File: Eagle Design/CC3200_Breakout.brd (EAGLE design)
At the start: 58.4 x 35.2 mm, 46 parts, among them J22 M10X2, J23 M10X2, U15 AT25FS010, Y2 32.768KHz, Y3 407MHz

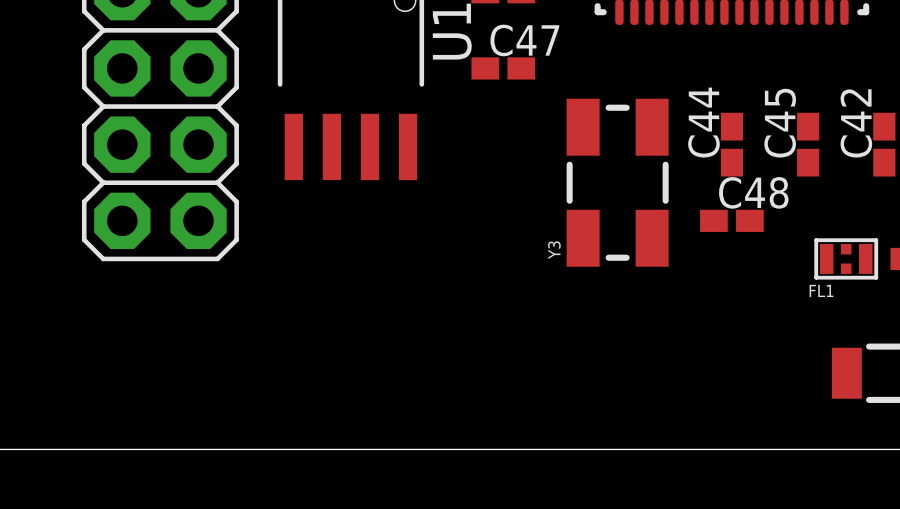
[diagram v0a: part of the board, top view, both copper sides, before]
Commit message: Added JTAG and Lock Connectors
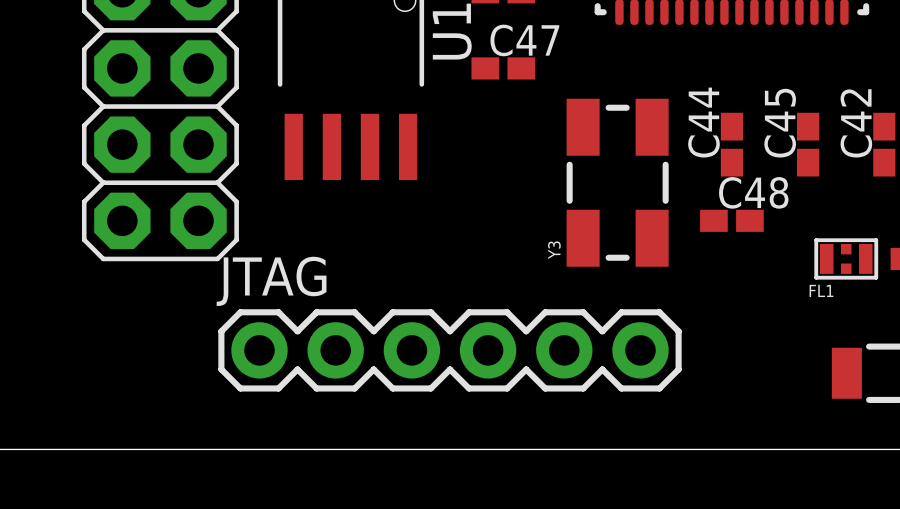
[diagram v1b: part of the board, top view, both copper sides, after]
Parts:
- added JTAG: (no value), SparkFun-Connectors:1X06
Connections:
- net GND: now also JTAG.2
- net JTAG_TCK: now also JTAG.3
- net JTAG_TDI: now also JTAG.5
- net JTAG_TDO: now also JTAG.6
- net JTAG_TMS: now also JTAG.4
- net VCC_BRD: now also JTAG.1
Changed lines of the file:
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@@
 <?xml version="1.0" encoding="utf-8"?>
 <!DOCTYPE eagle SYSTEM "eagle.dtd">
-<eagle version="6.4">
+<eagle version="7.1.0">
 <drawing>
 <settings>
@@
 <layer number="54" name="bGND_GNDA" color="1" fill="9" visible="no" active="no"/>
 <layer number="56" name="wert" color="7" fill="1" visible="no" active="no"/>
+<layer number="57" name="tCAD" color="7" fill="1" visible="no" active="no"/>
+<layer number="90" name="Modules" color="5" fill="1" visible="no" active="no"/>
 <layer number="91" name="Nets" color="2" fill="1" visible="no" active="no"/>
 <layer number="92" name="Busses" color="1" fill="1" visible="no" active="no"/>
@@
 <layer number="97" name="Info" color="7" fill="1" visible="no" active="no"/>
 <layer number="98" name="Guide" color="6" fill="1" visible="no" active="no"/>
+<layer number="99" name="SpiceOrder" color="7" fill="1" visible="no" active="no"/>
 <layer number="100" name="Muster" color="7" fill="1" visible="no" active="no"/>
 <layer number="101" name="Patch_Top" color="12" fill="4" visible="no" active="yes"/>
@@
 <layer number="108" name="tplace-old" color="10" fill="1" visible="yes" active="yes"/>
 <layer number="109" name="ref-old" color="11" fill="1" visible="yes" active="yes"/>
+<layer number="110" name="fp0" color="7" fill="1" visible="yes" active="yes"/>
+<layer number="111" name="LPC17xx" color="7" fill="1" visible="yes" active="yes"/>
+<layer number="112" name="tSilk" color="7" fill="1" visible="yes" active="yes"/>
+<layer number="113" name="IDFDebug" color="4" fill="1" visible="yes" active="yes"/>
 <layer number="116" name="Patch_BOT" color="9" fill="4" visible="no" active="yes"/>
 <layer number="121" name="_tsilk" color="7" fill="1" visible="no" active="yes"/>
 <layer number="122" name="_bsilk" color="7" fill="1" visible="no" active="yes"/>
+<layer number="123" name="tTestmark" color="7" fill="1" visible="yes" active="yes"/>
+<layer number="124" name="bTestmark" color="7" fill="1" visible="yes" active="yes"/>
 <layer number="125" name="_tNames" color="7" fill="1" visible="no" active="yes"/>
+<layer number="126" name="_bNames" color="7" fill="1" visible="yes" active="yes"/>
+<layer number="127" name="_tValues" color="7" fill="1" visible="yes" active="yes"/>
+<layer number="128" name="_bValues" color="7" fill="1" visible="yes" active="yes"/>
+<layer number="131" name="tAdjust" color="7" fill="1" visible="yes" active="yes"/>
+<layer number="132" name="bAdjust" color="7" fill="1" visible="yes" active="yes"/>
 <layer number="144" name="Drill_legend" color="7" fill="1" visible="no" active="yes"/>
+<layer number="150" name="Notes" color="7" fill="1" visible="yes" active="yes"/>
 <layer number="151" name="HeatSink" color="7" fill="1" visible="no" active="yes"/>
+<layer number="152" name="_bDocu" color="7" fill="1" visible="yes" active="yes"/>
+<layer number="153" name="FabDoc1" color="7" fill="1" visible="yes" active="yes"/>
+<layer number="154" name="FabDoc2" color="7" fill="1" visible="yes" active="yes"/>
+<layer number="155" name="FabDoc3" color="7" fill="1" visible="yes" active="yes"/>
 <layer number="199" name="Contour" color="7" fill="1" visible="no" active="yes"/>
 <layer number="200" name="200bmp" color="1" fill="10" visible="no" active="yes"/>
@@
 <layer number="223" name="223bmp" color="24" fill="1" visible="no" active="no"/>
 <layer number="224" name="224bmp" color="25" fill="1" visible="no" active="no"/>
+<layer number="248" name="Housing" color="7" fill="1" visible="yes" active="yes"/>
+<layer number="249" name="Edge" color="7" fill="1" visible="yes" active="yes"/>
 <layer number="250" name="Descript" color="3" fill="1" visible="no" active="no"/>
 <layer number="251" name="SMDround" color="12" fill="11" visible="no" active="no"/>
@@
 <pass name="Default">
 <param name="RoutingGrid" value="50mil"/>
+<param name="AutoGrid" value="1"/>
+<param name="Efforts" value="0"/>
+<param name="TopRouterVariant" value="1"/>
 <param name="tpViaShape" value="round"/>
 <param name="PrefDir.1" value="|"/>
@@
 <element name="Y2" library="SparkFun-FreqCtrl" package="CRYSTAL-SMD-5X3" value="32.768KHz" x="21.59" y="29.21"/>
 <element name="Y3" library="SparkFun-FreqCtrl" package="CRYSTAL-SMD-5X3" value="407MHz" x="22.86" y="8.89" rot="R90"/>
+<element name="JTAG" library="SparkFun-Connectors" package="1X06" value="" x="10.922" y="3.302">
+<attribute name="PROD_ID" value="CONN-08437" x="10.922" y="3.302" size="1.778" layer="27" display="off"/>
+</element>
 </elements>
 <signals>
@@
 <signal name="JTAG_TDO">
 <contactref element="U$1" pad="17"/>
+<contactref element="JTAG" pad="6"/>
+<wire x1="23.622" y1="3.302" x2="22.92" y2="14.575" width="0" layer="19" extent="1-1"/>
 </signal>
 <signal name="JTAG_TDI">
 <contactref element="U$1" pad="16"/>
+<contactref element="JTAG" pad="5"/>
+<wire x1="21.082" y1="3.302" x2="22.195" y2="15.3" width="0" layer="19" extent="1-1"/>
 </signal>
 <signal name="JTAG_TMS">
 <contactref element="U$1" pad="20"/>
+<contactref element="JTAG" pad="4"/>
+<wire x1="18.542" y1="3.302" x2="24.42" y2="14.575" width="0" layer="19" extent="1-1"/>
 </signal>
 <signal name="JTAG_TCK">
 <contactref element="U$1" pad="19"/>
+<contactref element="JTAG" pad="3"/>
+<wire x1="16.002" y1="3.302" x2="23.92" y2="14.575" width="0" layer="19" extent="1-1"/>
 </signal>
 <signal name="GND">
@@
 <contactref element="J22" pad="4"/>
 <contactref element="J23" pad="2"/>
+<contactref element="JTAG" pad="2"/>
 <wire x1="47.082" y1="30.48" x2="52.07" y2="30.48" width="0" layer="19" extent="1-1"/>
 <wire x1="46.736" y1="27.27" x2="47.082" y2="30.48" width="0" layer="19" extent="1-1"/>
@@
 <wire x1="16.51" y1="29.81" x2="14.57" y2="22.86" width="0" layer="19" extent="1-1"/>
 <wire x1="8.89" y1="27.94" x2="14.57" y2="22.86" width="0" layer="19" extent="1-1"/>
+<wire x1="13.462" y1="3.302" x2="19.65" y2="12.7" width="0" layer="19" extent="1-1"/>
 </signal>
 <signal name="N$5">
@@
 <signal name="VCC_BRD">
 <contactref element="J22" pad="1"/>
+<contactref element="JTAG" pad="1"/>
+<wire x1="10.922" y1="3.302" x2="6.35" y2="30.48" width="0" layer="19" extent="1-1"/>
 </signal>
 <signal name="58">
